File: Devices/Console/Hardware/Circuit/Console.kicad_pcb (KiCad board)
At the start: 2 copper layers, 96.8 x 62 mm, 35 parts, among them J1 AVR-ISP-6, J2 TYPE-C-31-M-12, J3 Conn_01x13, J4 Conn_01x04, J5 Conn_01x04, SW1 PEC11R-4220F-S0012, SW2 PEC11R-4220F-S0012, SW3 PEC11R-4220F-S0012, SW4 PEC11R-4220F-S0012, SW5 SW_Push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

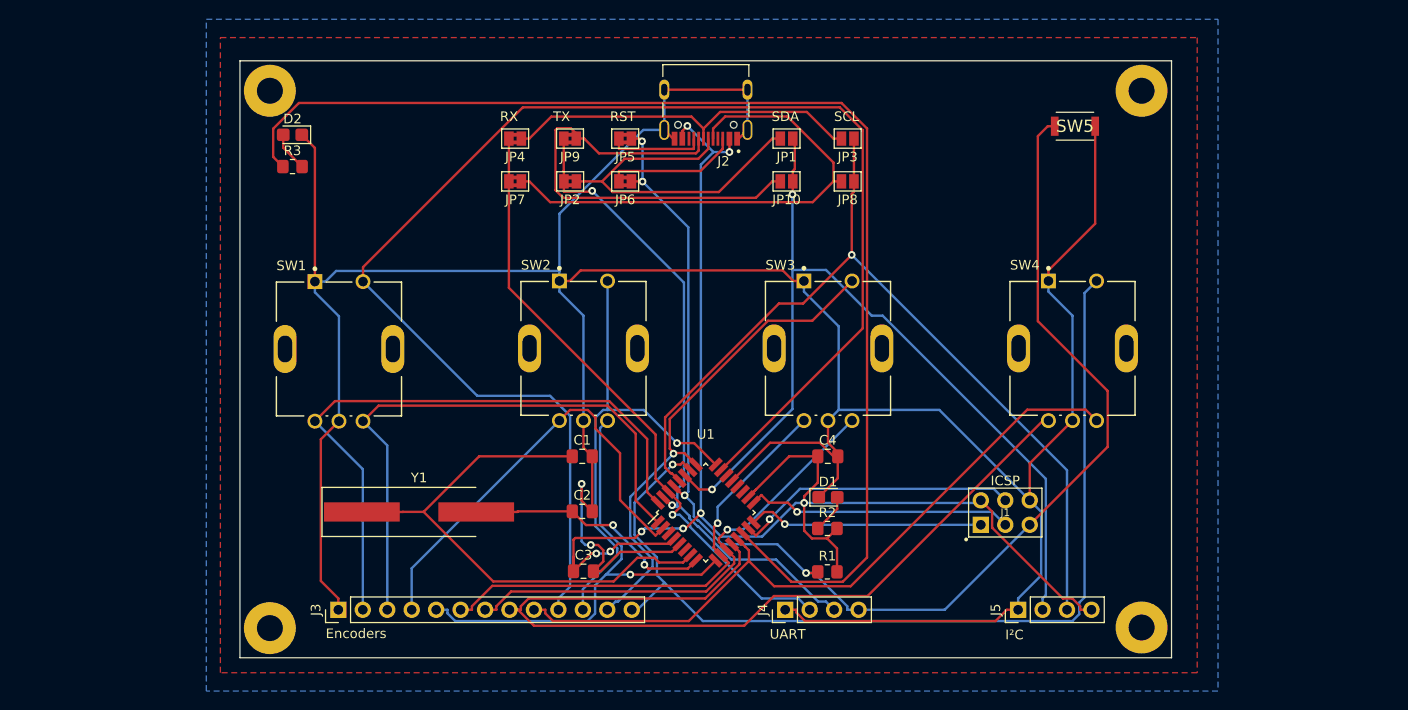
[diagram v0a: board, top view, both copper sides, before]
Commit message: Bigger spacing between encoders
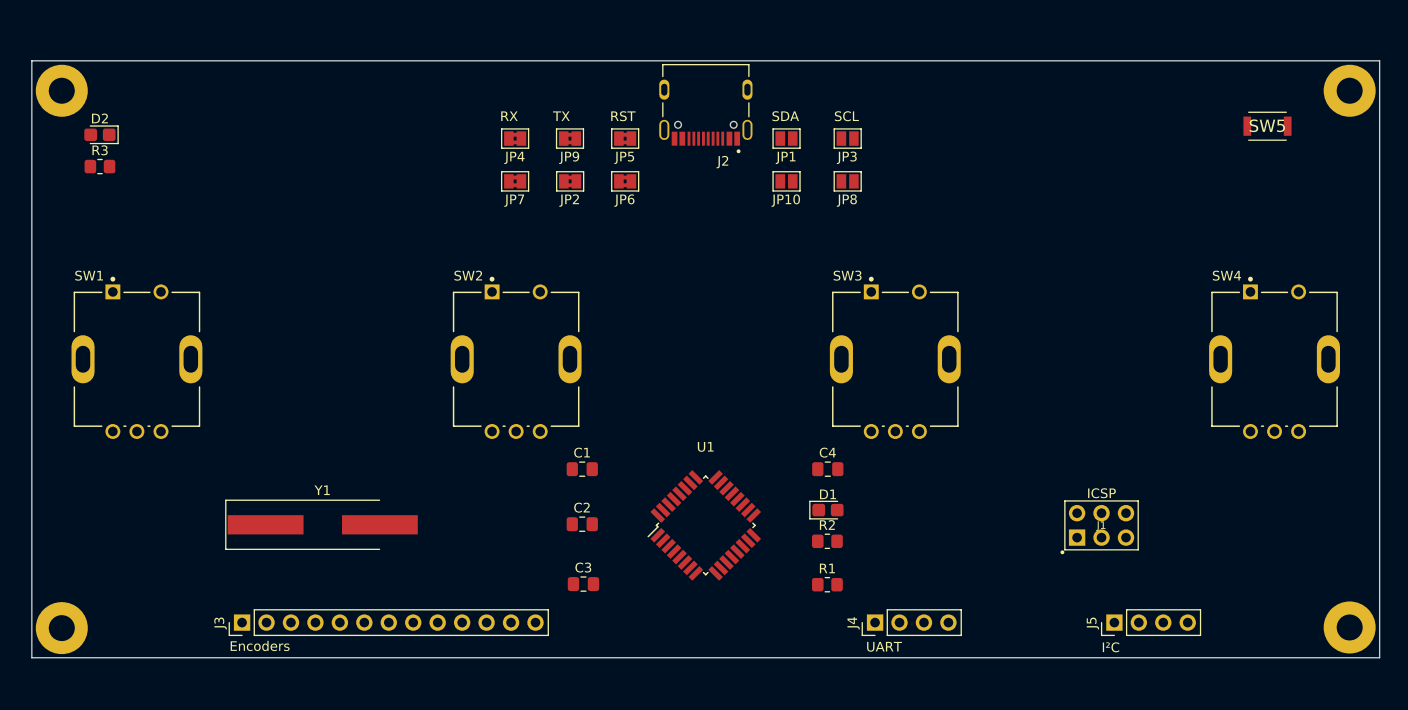
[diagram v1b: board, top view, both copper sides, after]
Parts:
- moved PAD1 21.6 mm to (79.3, 67.9)
- moved PAD2 21.6 mm to (213.1, 67.9)
- moved PAD3 21.6 mm to (79.3, 123.7)
- moved PAD4 21.6 mm to (213.1, 123.6)
- moved SW4 21.0 mm to (205.3, 95.8)
- moved SW1 21.0 mm to (87.2, 95.8)
- moved D2 20.0 mm to (83.3, 72.5)
- moved R3 20.0 mm to (83.3, 75.8)
- moved SW5 20.0 mm to (204.6, 71.6)
- moved J1 10.1 mm to (187.4, 113.0)
- moved J3 10.1 mm to (98.1, 123.1)
- moved J5 10.1 mm to (188.7, 123.1)
- moved Y1 10.1 mm to (106.5, 113.0)
- moved J4 9.43 mm to (163.8, 123.1)
- moved SW3 7.09 mm to (165.9, 95.8)
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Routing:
- net GND: track 340.6 -> 0.00 mm, vias 2 -> 0
- net VCC: track 154.1 -> 0.00 mm, vias 8 -> 0
- net BTN1: track 150.6 -> 0.00 mm
- net RST: track 138.3 -> 0.00 mm, vias 4 -> 0
- net LED: track 128.8 -> 0.00 mm
- net BTN4: track 102.4 -> 0.00 mm, vias 1 -> 0
- net ENC4A: track 93.1 -> 0.00 mm
- net SDA: track 92.7 -> 0.00 mm, vias 2 -> 0
- net SCL: track 92.0 -> 0.00 mm, vias 1 -> 0
- net ENC4B: track 73.7 -> 0.00 mm
- net TX: track 68.3 -> 0.00 mm, vias 2 -> 0
- net ENC1A: track 65.7 -> 0.00 mm
- net RX: track 65.2 -> 0.00 mm, vias 1 -> 0
- net ENC1B: track 61.0 -> 0.00 mm
- net XTAL1: track 56.5 -> 0.00 mm
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- removed copper zone on B.Cu, net GND
- removed copper zone on F.Cu, net GND
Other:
- board size 96.8 x 62 mm -> 140 x 62 mm

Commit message: Wider encoder gap pcb traces
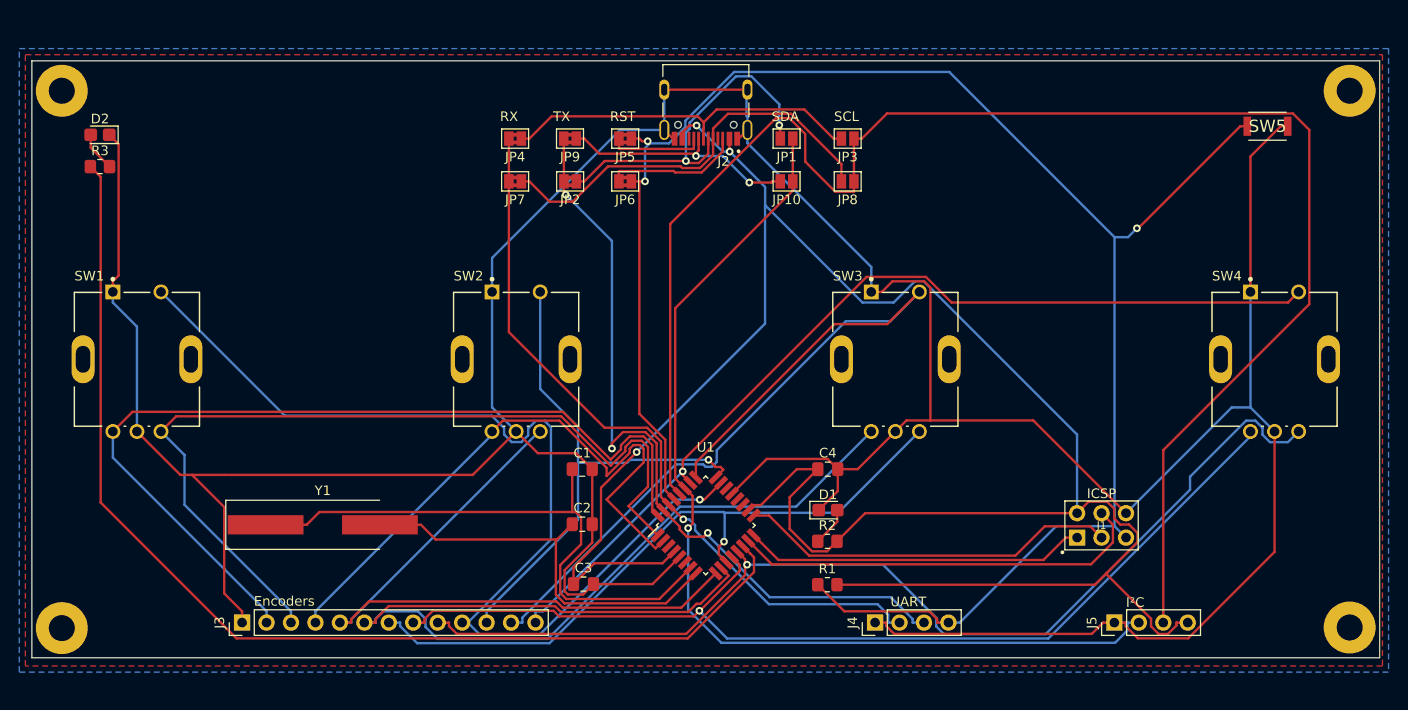
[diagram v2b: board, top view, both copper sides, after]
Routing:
- net GND: track 0.00 -> 401.6 mm
- net VCC: track 0.00 -> 231.0 mm, vias 0 -> 3
- net RST: track 0.00 -> 188.1 mm, vias 0 -> 3
- net SCL: track 0.00 -> 169.0 mm
- net LED: track 0.00 -> 115.1 mm
- net ENC4B: track 0.00 -> 110.7 mm, vias 0 -> 1
- net BTN1: track 0.00 -> 106.7 mm, vias 0 -> 1
- net ENC4A: track 0.00 -> 106.2 mm, vias 0 -> 1
- net ENC3A: track 0.00 -> 105.7 mm
- net SDA: track 0.00 -> 104.5 mm, vias 0 -> 1
- net BTN4: track 0.00 -> 98.6 mm, vias 0 -> 1
- net ENC1A: track 0.00 -> 94.6 mm
- net ENC1B: track 0.00 -> 91.7 mm
- net BTN3: track 0.00 -> 90.0 mm
- net TX: track 0.00 -> 80.5 mm, vias 0 -> 3
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- added copper zone on B.Cu, net GND
- added copper zone on F.Cu, net GND

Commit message: Plot Gerber files
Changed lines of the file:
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@@
       (outputformat 1)
       (mirror false)
-      (drillshape 1)
+      (drillshape 0)
       (scaleselection 1)
-      (outputdirectory ""))
+      (outputdirectory "Gerber/"))
   )
   (net 0 "")
@@
       (effects (font (size 0.5 0.5) (thickness 0.08)))
     )
-    (pad 1 smd roundrect (at -1.0375 0) (size 1.175 1.45) (layers F.Cu F.Paste F.Mask) (roundrect_rratio 0.212766)
+    (pad 1 smd roundrect (at -1.0375 0) (size 1.175 1.45) (layers F.Cu F.Paste F.Mask) (roundrect_rratio 0.2127659574468085)
       (net 6 XTAL1))
-    (pad 2 smd roundrect (at 1.0375 0) (size 1.175 1.45) (layers F.Cu F.Paste F.Mask) (roundrect_rratio 0.212766)
+    (pad 2 smd roundrect (at 1.0375 0) (size 1.175 1.45) (layers F.Cu F.Paste F.Mask) (roundrect_rratio 0.2127659574468085)
       (net 4 GND))
     (model ${KISYS3DMOD}/Capacitor_SMD.3dshapes/C_0805_2012Metric.wrl
@@
       (effects (font (size 0.5 0.5) (thickness 0.08)))
     )
-    (pad 2 smd roundrect (at 1.0375 0) (size 1.175 1.45) (layers F.Cu F.Paste F.Mask) (roundrect_rratio 0.212766)
-      (net 4 GND))
-    (pad 1 smd roundrect (at -1.0375 0) (size 1.175 1.45) (layers F.Cu F.Paste F.Mask) (roundrect_rratio 0.212766)
+    (pad 2 smd roundrect (at 1.0375 0) (size 1.175 1.45) (layers F.Cu F.Paste F.Mask) (roundrect_rratio 0.2127659574468085)
+      (net 4 GND))
+    (pad 1 smd roundrect (at -1.0375 0) (size 1.175 1.45) (layers F.Cu F.Paste F.Mask) (roundrect_rratio 0.2127659574468085)
       (net 7 XTAL2))
     (model ${KISYS3DMOD}/Capacitor_SMD.3dshapes/C_0805_2012Metric.wrl
@@
       (effects (font (size 0.5 0.5) (thickness 0.08)))
     )
-    (pad 1 smd roundrect (at -1 0) (size 1.2 1.4) (layers F.Cu F.Paste F.Mask) (roundrect_rratio 0.208333)
+    (pad 1 smd roundrect (at -1 0) (size 1.2 1.4) (layers F.Cu F.Paste F.Mask) (roundrect_rratio 0.2083325)
       (net 8 "Net-(D1-Pad2)"))
-    (pad 2 smd roundrect (at 1 0) (size 1.2 1.4) (layers F.Cu F.Paste F.Mask) (roundrect_rratio 0.208333)
+    (pad 2 smd roundrect (at 1 0) (size 1.2 1.4) (layers F.Cu F.Paste F.Mask) (roundrect_rratio 0.2083325)
       (net 5 VCC))
     (model ${KISYS3DMOD}/Resistor_SMD.3dshapes/R_0805_2012Metric.wrl
@@
       (effects (font (size 0.5 0.5) (thickness 0.08)))
     )
-    (pad 1 smd roundrect (at -0.9625 0) (size 1.325 1.3) (layers F.Cu F.Paste F.Mask) (roundrect_rratio 0.192308)
-      (net 4 GND))
-    (pad 2 smd roundrect (at 0.9625 0) (size 1.325 1.3) (layers F.Cu F.Paste F.Mask) (roundrect_rratio 0.192308)
+    (pad 1 smd roundrect (at -0.9625 0) (size 1.325 1.3) (layers F.Cu F.Paste F.Mask) (roundrect_rratio 0.1923076923076923)
+      (net 4 GND))
+    (pad 2 smd roundrect (at 0.9625 0) (size 1.325 1.3) (layers F.Cu F.Paste F.Mask) (roundrect_rratio 0.1923076923076923)
       (net 8 "Net-(D1-Pad2)"))
     (model ${KISYS3DMOD}/LED_SMD.3dshapes/LED_0805_2012Metric_Castellated.wrl
@@
       (effects (font (size 0.5 0.5) (thickness 0.08)))
     )
-    (pad 1 smd roundrect (at -1.0375 0) (size 1.175 1.45) (layers F.Cu F.Paste F.Mask) (roundrect_rratio 0.212766)
+    (pad 1 smd roundrect (at -1.0375 0) (size 1.175 1.45) (layers F.Cu F.Paste F.Mask) (roundrect_rratio 0.2127659574468085)
       (net 5 VCC))
-    (pad 2 smd roundrect (at 1.0375 0) (size 1.175 1.45) (layers F.Cu F.Paste F.Mask) (roundrect_rratio 0.212766)
+    (pad 2 smd roundrect (at 1.0375 0) (size 1.175 1.45) (layers F.Cu F.Paste F.Mask) (roundrect_rratio 0.2127659574468085)
       (net 4 GND))
     (model ${KISYS3DMOD}/Capacitor_SMD.3dshapes/C_0805_2012Metric.wrl
@@
       (effects (font (size 0.5 0.5) (thickness 0.08)))
     )
-    (pad 1 smd roundrect (at -1 0) (size 1.2 1.4) (layers F.Cu F.Paste F.Mask) (roundrect_rratio 0.208333)
+    (pad 1 smd roundrect (at -1 0) (size 1.2 1.4) (layers F.Cu F.Paste F.Mask) (roundrect_rratio 0.2083325)
       (net 12 RST))
-    (pad 2 smd roundrect (at 1 0) (size 1.2 1.4) (layers F.Cu F.Paste F.Mask) (roundrect_rratio 0.208333)
+    (pad 2 smd roundrect (at 1 0) (size 1.2 1.4) (layers F.Cu F.Paste F.Mask) (roundrect_rratio 0.2083325)
       (net 5 VCC))
     (model ${KISYS3DMOD}/Resistor_SMD.3dshapes/R_0805_2012Metric.wrl
@@
       (effects (font (size 0.5 0.5) (thickness 0.08)))
     )
-    (pad 1 smd roundrect (at -0.9625 0 180) (size 1.325 1.3) (layers F.Cu F.Paste F.Mask) (roundrect_rratio 0.192308)
-      (net 4 GND))
-    (pad 2 smd roundrect (at 0.9625 0 180) (size 1.325 1.3) (layers F.Cu F.Paste F.Mask) (roundrect_rratio 0.192308)
+    (pad 1 smd roundrect (at -0.9625 0 180) (size 1.325 1.3) (layers F.Cu F.Paste F.Mask) (roundrect_rratio 0.1923076923076923)
+      (net 4 GND))
+    (pad 2 smd roundrect (at 0.9625 0 180) (size 1.325 1.3) (layers F.Cu F.Paste F.Mask) (roundrect_rratio 0.1923076923076923)
       (net 37 "Net-(D2-Pad2)"))
     (model ${KISYS3DMOD}/LED_SMD.3dshapes/LED_0805_2012Metric_Castellated.wrl
@@
       (effects (font (size 0.5 0.5) (thickness 0.08)))
     )
-    (pad 1 smd roundrect (at -1 0 180) (size 1.2 1.4) (layers F.Cu F.Paste F.Mask) (roundrect_rratio 0.208333)
+    (pad 1 smd roundrect (at -1 0 180) (size 1.2 1.4) (layers F.Cu F.Paste F.Mask) (roundrect_rratio 0.2083325)
       (net 37 "Net-(D2-Pad2)"))
-    (pad 2 smd roundrect (at 1 0 180) (size 1.2 1.4) (layers F.Cu F.Paste F.Mask) (roundrect_rratio 0.208333)
+    (pad 2 smd roundrect (at 1 0 180) (size 1.2 1.4) (layers F.Cu F.Paste F.Mask) (roundrect_rratio 0.2083325)
       (net 38 LED))
     (model ${KISYS3DMOD}/Resistor_SMD.3dshapes/R_0805_2012Metric.wrl
@@
       (effects (font (size 0.5 0.5) (thickness 0.08)))
     )
-    (pad 1 smd roundrect (at -1.0375 0) (size 1.175 1.45) (layers F.Cu F.Paste F.Mask) (roundrect_rratio 0.212766)
+    (pad 1 smd roundrect (at -1.0375 0) (size 1.175 1.45) (layers F.Cu F.Paste F.Mask) (roundrect_rratio 0.2127659574468085)
       (net 5 VCC))
-    (pad 2 smd roundrect (at 1.0375 0) (size 1.175 1.45) (layers F.Cu F.Paste F.Mask) (roundrect_rratio 0.212766)
+    (pad 2 smd roundrect (at 1.0375 0) (size 1.175 1.45) (layers F.Cu F.Paste F.Mask) (roundrect_rratio 0.2127659574468085)
       (net 4 GND))
     (model ${KISYS3DMOD}/Capacitor_SMD.3dshapes/C_0805_2012Metric.wrl

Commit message: Generate Gerbers
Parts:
- moved D2 19.0 mm to (102.3, 72.5)
- moved PAD1 19.0 mm to (98.3, 67.9)
- moved PAD2 19.0 mm to (194.1, 67.9)
- moved PAD3 19.0 mm to (98.3, 123.7)
- moved PAD4 19.0 mm to (194.1, 123.6)
- moved R3 19.0 mm to (102.3, 75.8)
- moved SW5 19.0 mm to (185.6, 71.6)
- moved SW1 16.0 mm to (103.1, 95.8)
- moved SW4 16.0 mm to (189.4, 95.8)
- moved J1 10.0 mm to (177.4, 113.0)
- moved J3 10.0 mm to (108.1, 123.1)
- moved J4 10.0 mm to (153.8, 123.1)
- moved J5 10.0 mm to (178.7, 123.1)
- moved Y1 10.0 mm to (116.5, 113.0)
- moved SW3 5.32 mm to (160.6, 95.8)
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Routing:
- net GND: track 401.6 -> 359.8 mm, vias 0 -> 1
- net RST: track 188.1 -> 147.5 mm, vias 3 -> 2
- net BTN3: track 90.0 -> 49.7 mm, vias 0 -> 1
- net SCL: track 169.0 -> 132.2 mm
- net ENC1B: track 91.7 -> 65.2 mm
- net ENC1A: track 94.6 -> 69.8 mm
- net BTN1: track 106.7 -> 85.2 mm
- net ENC3B: track 71.1 -> 52.0 mm
- net BTN4: track 98.6 -> 80.0 mm
- net ENC3A: track 105.7 -> 121.3 mm
- net ENC2B: track 71.1 -> 57.9 mm
- net TX: track 80.5 -> 68.0 mm, vias 3 -> 1
- net LED: track 115.1 -> 103.2 mm
- net ENC2A: track 63.5 -> 51.7 mm, vias 0 -> 1
- net MOSI: track 43.4 -> 33.3 mm
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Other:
- board size 140 x 62 mm -> 102 x 62 mm

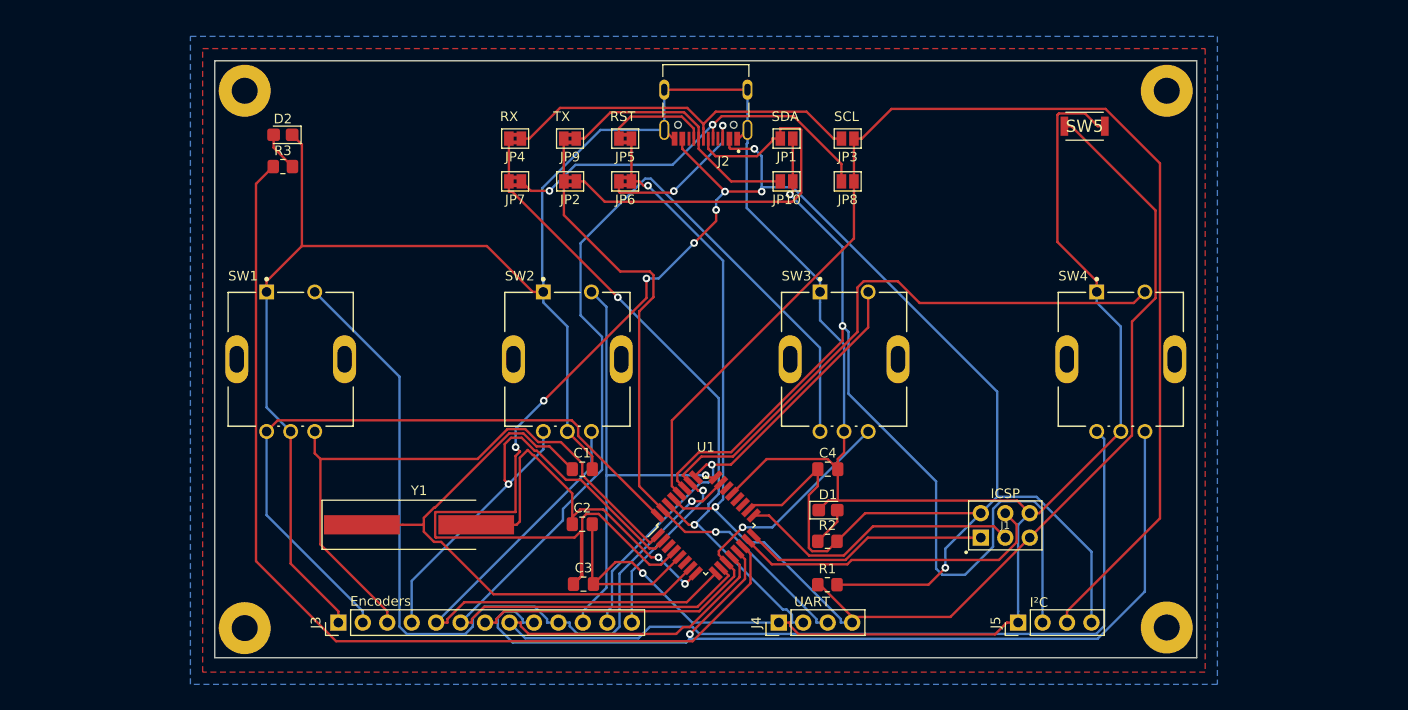
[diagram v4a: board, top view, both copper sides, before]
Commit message: Add UART/I2C pull-up resistors
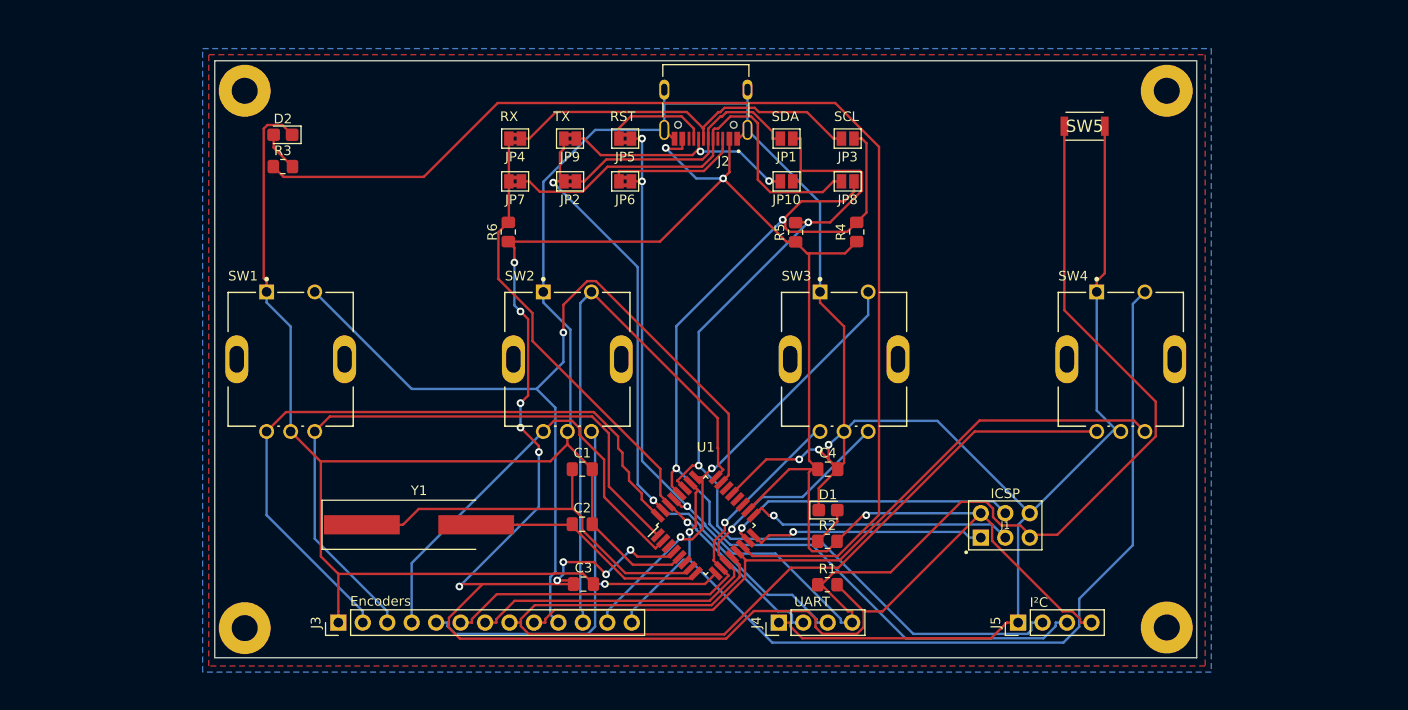
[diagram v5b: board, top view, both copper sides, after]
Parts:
- added R4: 10k, Resistor_SMD:R_0805_2012Metric_Pad1.20x1.40mm_HandSolder, F.Cu at (161.9, 82.5)
- added R5: 10k, Resistor_SMD:R_0805_2012Metric_Pad1.20x1.40mm_HandSolder, F.Cu at (155.6, 82.6)
- added R6: 10k, Resistor_SMD:R_0805_2012Metric_Pad1.20x1.40mm_HandSolder, F.Cu at (125.7, 82.5)
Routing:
- net ENC3A: track 121.3 -> 50.6 mm, vias 0 -> 1
- net VCC: track 237.3 -> 280.1 mm, vias 9 -> 13
- net ENC4B: track 104.2 -> 75.2 mm, vias 1 -> 0
- net BTN4: track 80.0 -> 100.4 mm
- net LED: track 103.2 -> 123.0 mm
- net SCL: track 132.2 -> 112.5 mm, vias 0 -> 2
- net XTAL1: track 60.0 -> 42.7 mm
- net Net-(J2-PadA6): track 44.2 -> 27.2 mm
- net ENC4A: track 113.6 -> 97.8 mm
- net XTAL2: track 39.7 -> 25.5 mm, vias 2 -> 0
- net BTN2: track 47.4 -> 60.2 mm, vias 1 -> 0
- net BTN1: track 85.2 -> 94.2 mm
- net ENC2B: track 57.9 -> 50.9 mm, vias 0 -> 1
- net GND: track 359.8 -> 366.5 mm, vias 1 -> 3
- net RST: track 147.5 -> 153.3 mm, vias 2 -> 3
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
